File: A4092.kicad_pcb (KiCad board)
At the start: 2 copper layers, 175.6 x 122.1 mm, 107 parts, among them CN1 Zorro3, J1 Conn_02x25_Odd_Even, J2 Conn_01x06_Pin, J3 TO-LED, J4 TO-MB, J5 5787170-5, J6 350543-1, J7 22112042, J8 TO-A3000-LED, J9 TO-A3000-MB, SW1 219-8MST, U1 SN74ABT16543DGGR, U10 SN74F244DB, U12 74LVC07APW_118, U13 SN74ABT16245ADGGR, U15 AMS1117-3.3, U16 XC95144XL-TQ144, U2 SN74ABT16543DGGR, U3 SN74ABT16543DGGR, U4 NCR53c710 SCSI Host Controller, U6 SN74ABT16543DGGR, U7 SST39SF010, U8 DS21S07A, U9 DS21S07A, Y1 Abracon ACO-50MHz

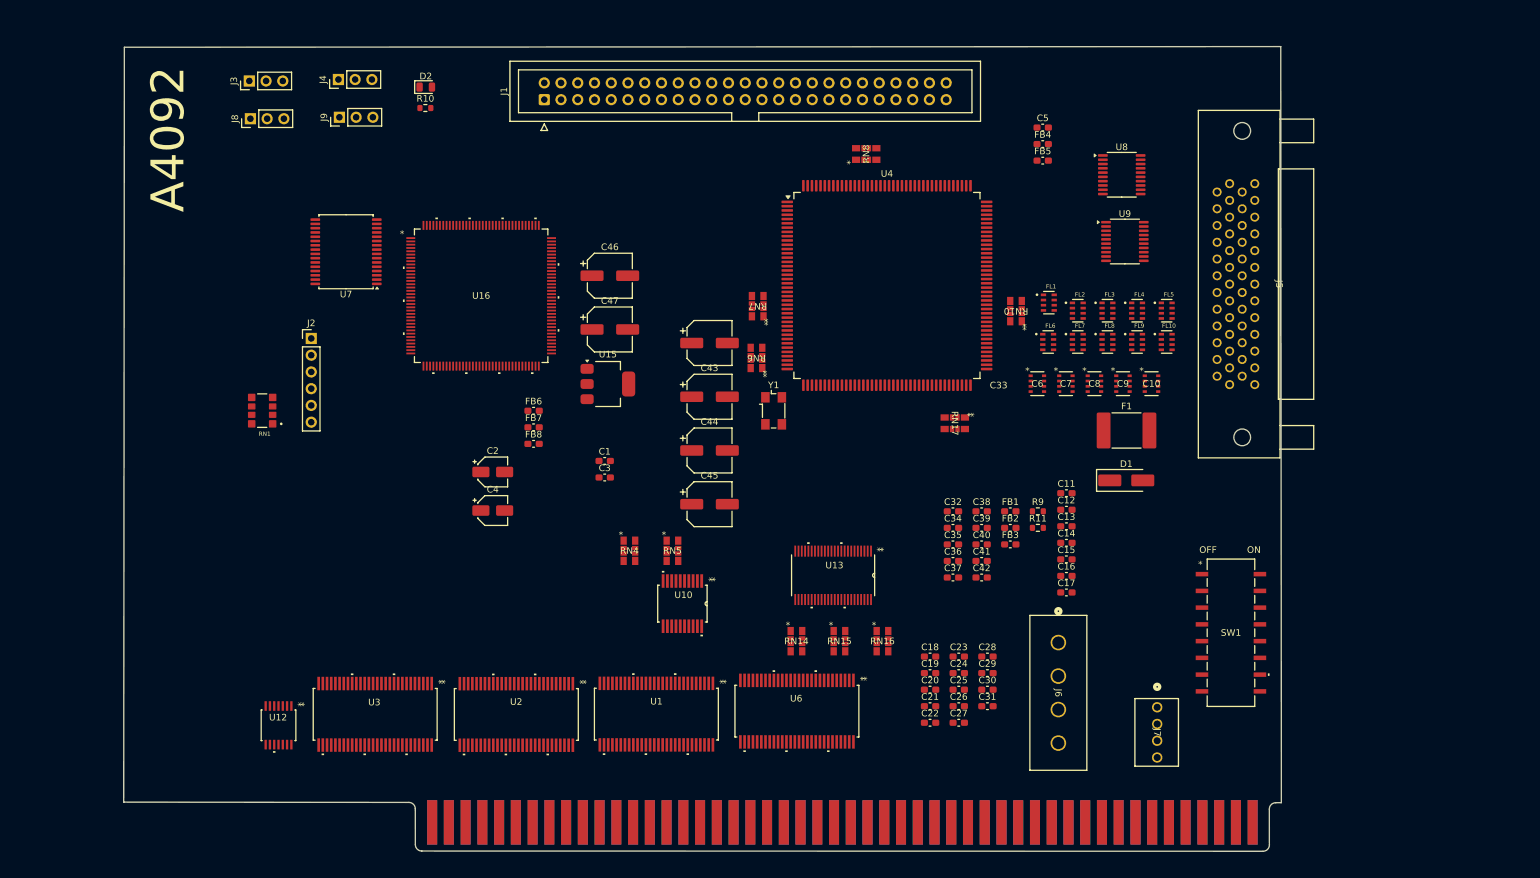
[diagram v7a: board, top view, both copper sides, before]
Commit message: 1. Placement looks feasible on 1 layer. Pending routing confirmation. 2. pages 1-2 placed. 3. components outside the outline are looking for a new home.
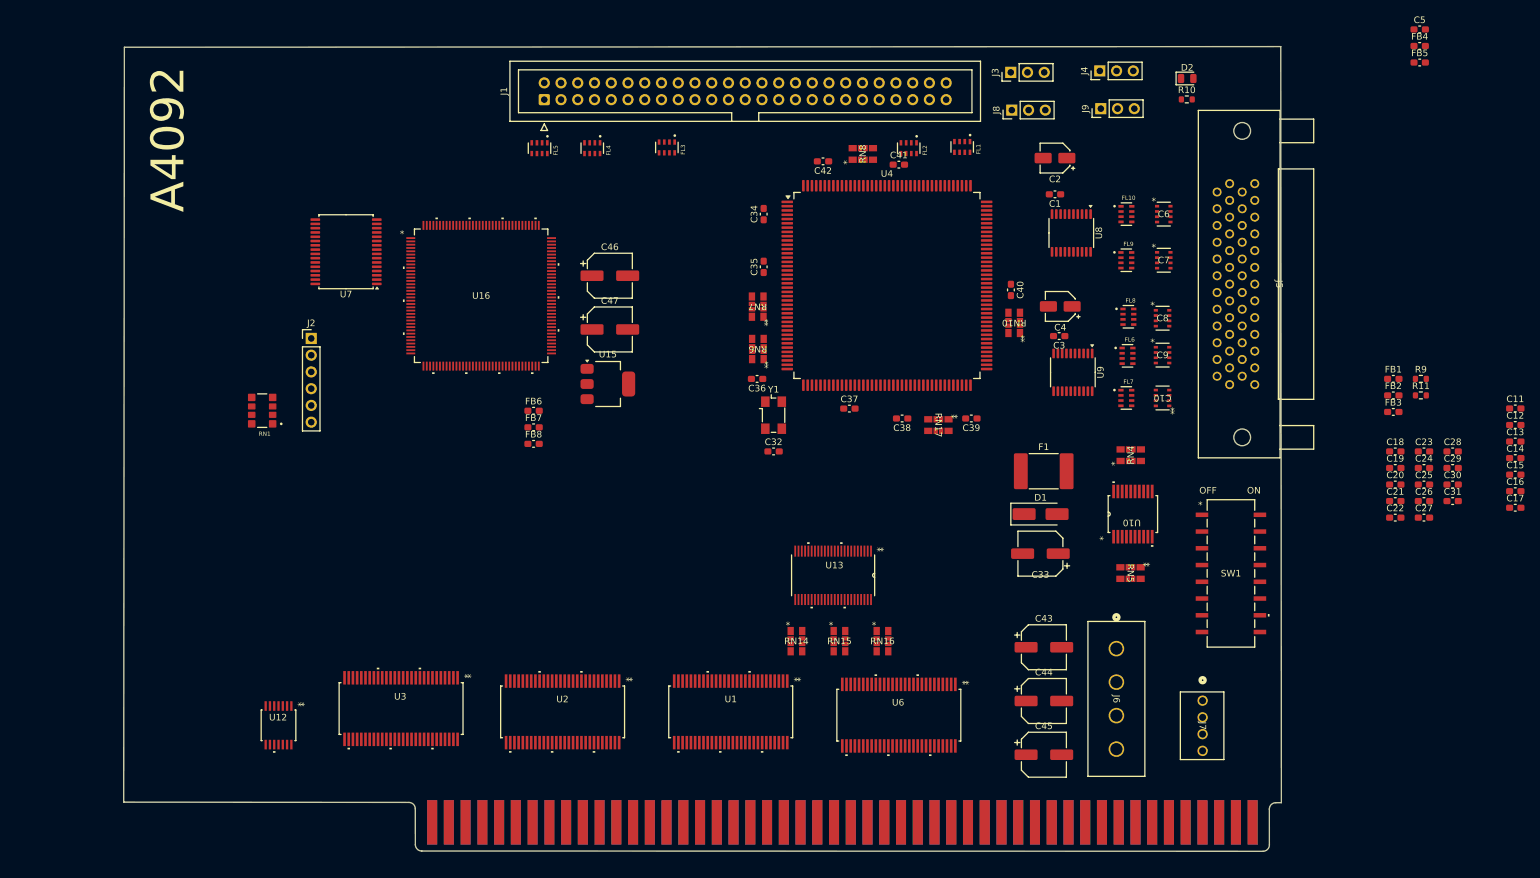
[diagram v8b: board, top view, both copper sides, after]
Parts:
- moved D2 115.5 mm to (210.2, 37.4)
- moved J4 115.5 mm to (197.0, 36.3)
- moved R10 115.5 mm to (210.2, 40.6)
- moved J3 115.5 mm to (183.5, 36.5)
- moved J8 115.5 mm to (183.6, 42.2)
- moved J9 115.5 mm to (197.1, 42.0)
- moved FL5 98.3 mm to (112.0, 48.0), turned to -90 degrees
- moved C2 97.7 mm to (190.2, 49.5), turned to 180 degrees
- moved C4 91.5 mm to (191.0, 72.0), turned to 180 degrees
- moved FL4 86.2 mm to (120.0, 48.0), turned to -90 degrees
- moved C1 79.4 mm to (190.2, 55.0), turned to 180 degrees
- moved RN4 77.4 mm to (201.7, 94.6), turned to 90 degrees
- moved C18 77.1 mm to (241.8, 94.0)
- moved C19 77.1 mm to (241.8, 96.5)
- moved C20 77.1 mm to (241.8, 99.0)
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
